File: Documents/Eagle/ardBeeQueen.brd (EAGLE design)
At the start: 54.8 x 57.1 mm, 12 parts

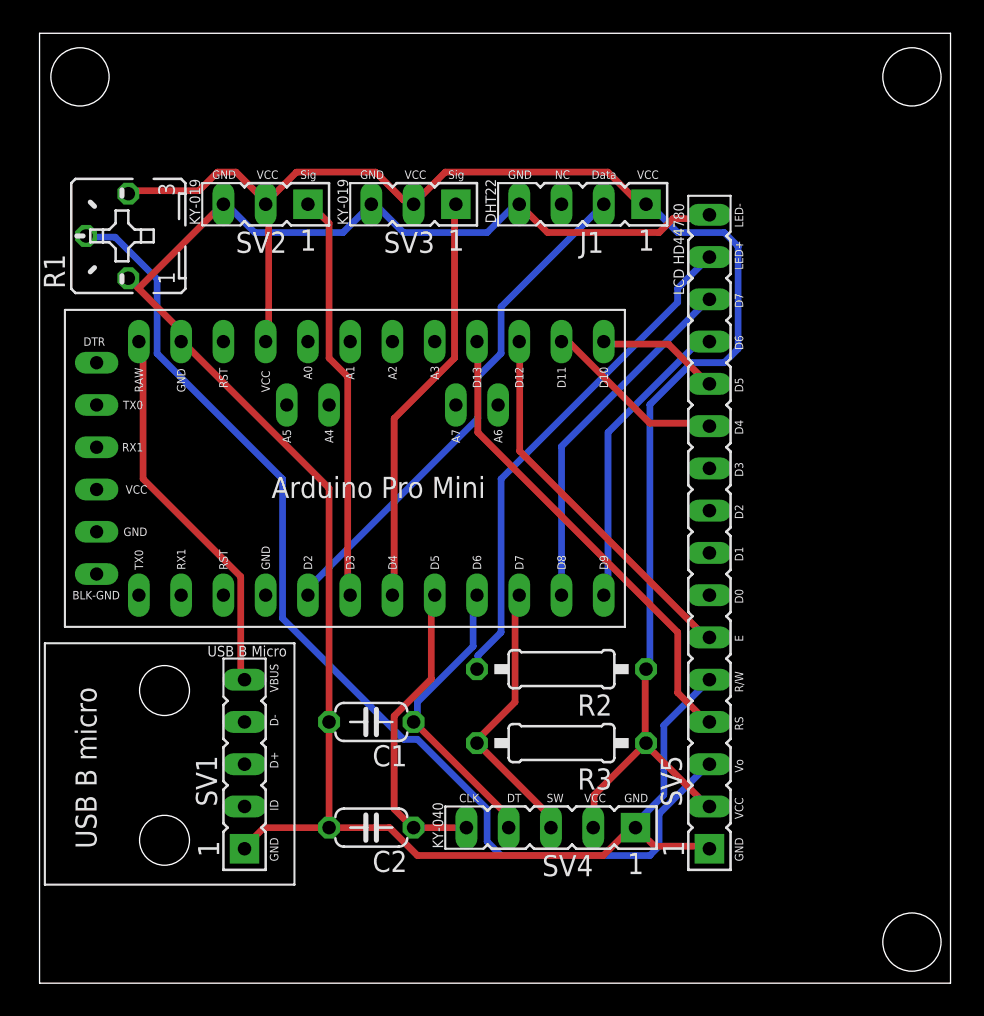
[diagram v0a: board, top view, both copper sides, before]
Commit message: updated eagle docs
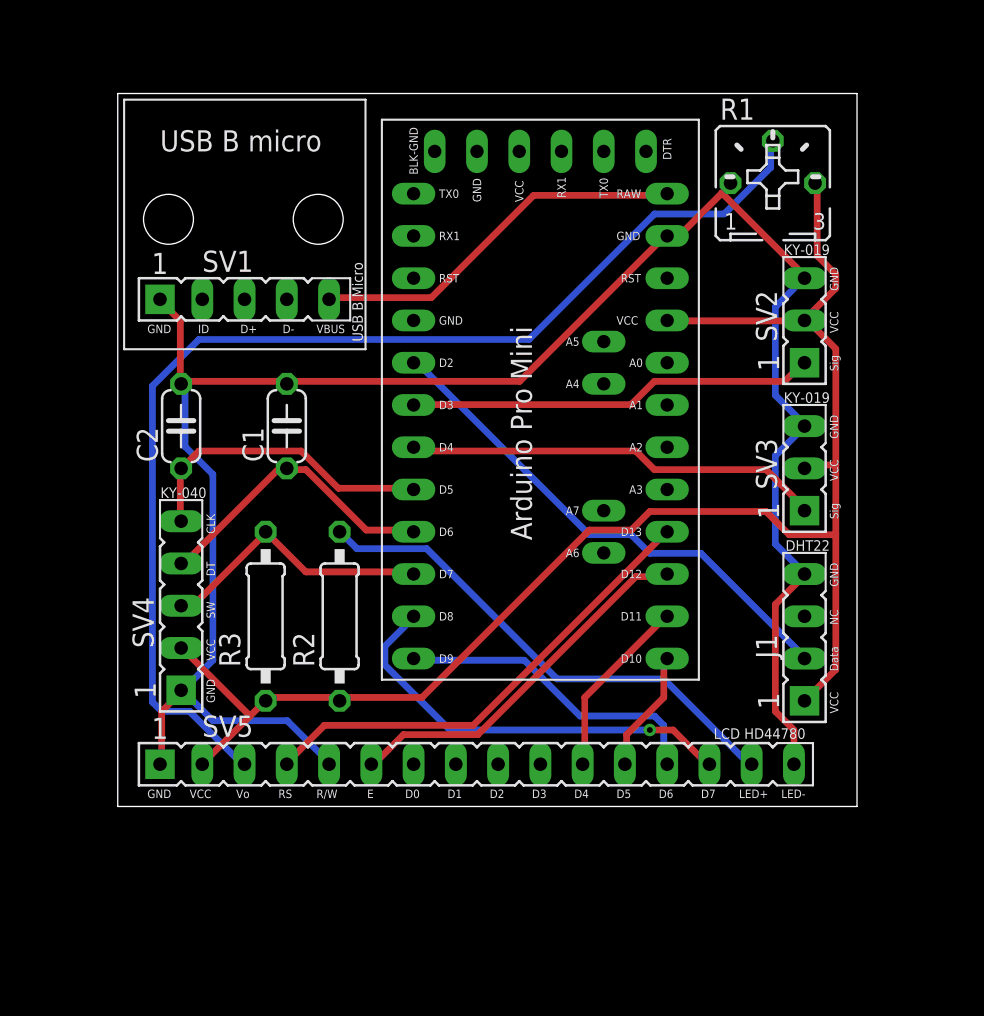
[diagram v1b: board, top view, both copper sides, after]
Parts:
- moved R1 38.9 mm to (40.6, 94.6), turned to 0 degrees
- moved SV2 36.3 mm to (42.5, 90.2), turned to 90 degrees
- moved SV3 29.9 mm to (42.5, 81.3), turned to 90 degrees
- moved J1 28.4 mm to (42.5, 69.8), turned to 90 degrees
- moved C2 26.7 mm to (5.08, 80.0), turned to 90 degrees
- moved SV1 26.7 mm to (10.2, 87.6), turned to 0 degrees
- moved SV4 25.5 mm to (5.08, 70.5), turned to 90 degrees
- moved SV5 21.0 mm to (27.9, 59.7), turned to 0 degrees
- moved R3 19.3 mm to (10.2, 68.6), turned to 90 degrees
- moved C1 18.5 mm to (11.4, 80.0), turned to 90 degrees
- moved R2 13.7 mm to (14.6, 68.6), turned to 90 degrees
- moved U$1 13.0 mm to (27.9, 81.3), turned to 0 degrees
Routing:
- net N$1: track 65.0 -> 70.3 mm
- net N$4: track 21.5 -> 25.6 mm, vias 0 -> 1
- net N$15: track 96.2 -> 95.3 mm
- net N$3: track 18.4 -> 19.1 mm
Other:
- board size 54.8 x 57.1 mm -> 44.4 x 42.9 mm

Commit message: upd
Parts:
- moved SV5 24.1 mm to (3.81, 59.7)
- moved SV2 6.35 mm to (42.5, 83.8)
- moved SV1 6.35 mm to (3.81, 87.6)
- moved J1 6.35 mm to (42.5, 63.5)
- moved SV3 6.35 mm to (42.5, 74.9)
- moved SV4 6.35 mm to (5.08, 64.1)
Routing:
- net N$1: track 70.3 -> 75.4 mm
- net N$16: track 120.0 -> 124.6 mm
- net N$8: track 28.7 -> 30.0 mm
- net N$15: track 95.3 -> 96.6 mm
